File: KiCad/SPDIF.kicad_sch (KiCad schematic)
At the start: 70 parts, among them J4 S/PDIF-Out, J5 S/PDIF-In1, J6 S/PDIF-In2, J7 S/PDIF-In3, T1 PE 65612, T2 PE 65612, T3 PE 65612, T4 PE 65612, U2 74HCU04, U3 MAX3490, U5 DIR9001, U6 DIR9001

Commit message: minor fixes
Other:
- note added: "C31 or C43 C44 or C32"
- note added: "C37 or C42 C41 or C38"
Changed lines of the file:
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@@
+		)
+	)
+	(rectangle
+		(start 128.27 57.15)
+		(end 189.23 72.39)
+		(stroke
+			(width 0)
+			(type default)
+		)
+		(fill
+			(type none)
+		)
+	)
+	(rectangle
+		(start 124.46 123.19)
+		(end 181.61 143.51)
+		(stroke
+			(width 0)
+			(type default)
+		)
+		(fill
+			(type none)
+		)
+	)
+	(text "C37 or C42\nC41 or C38"
+		(exclude_from_sim no)
+		(at 173.99 127 0)
+		(effects
+			(font
+				(size 1.27 1.27)
+			)
+		)
+	)
+	(text "C31 or C43\nC44 or C32"
+		(exclude_from_sim no)
+		(at 181.61 60.96 0)
+		(effects
+			(font
+				(size 1.27 1.27)
+			)
 		)
 	)

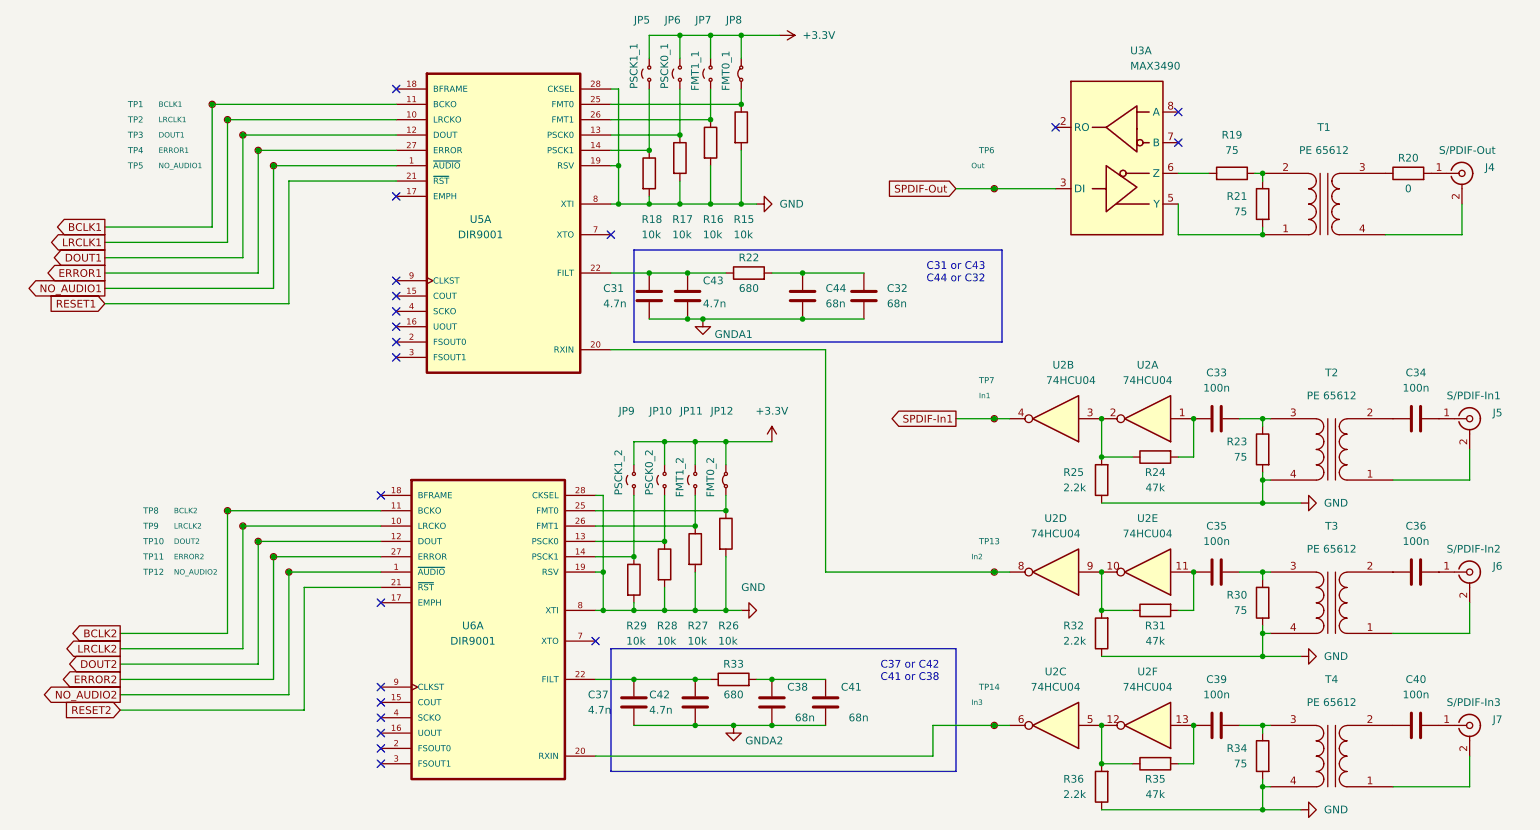
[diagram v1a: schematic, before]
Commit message: Minor and non-functional changes migration to KiCad 9
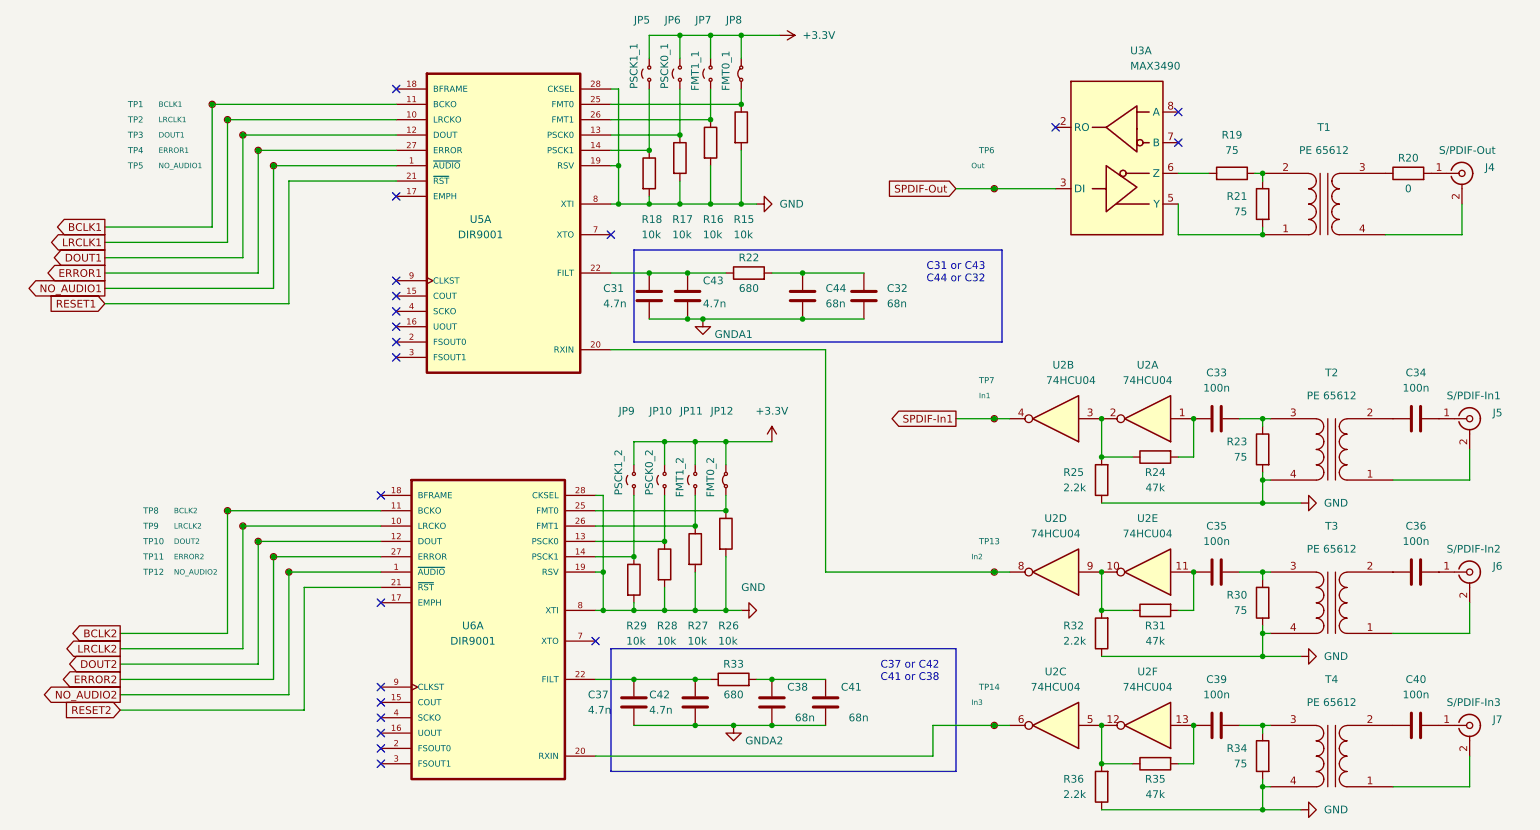
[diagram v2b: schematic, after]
